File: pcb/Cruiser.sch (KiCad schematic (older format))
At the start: 42 parts, among them J1 USB-A, P1 BDM, SW1 Load, SW2 Reset, T2 T2, T3 T3, U1 FT232RL, U2 MC9S12XDP512, X1 16MHz

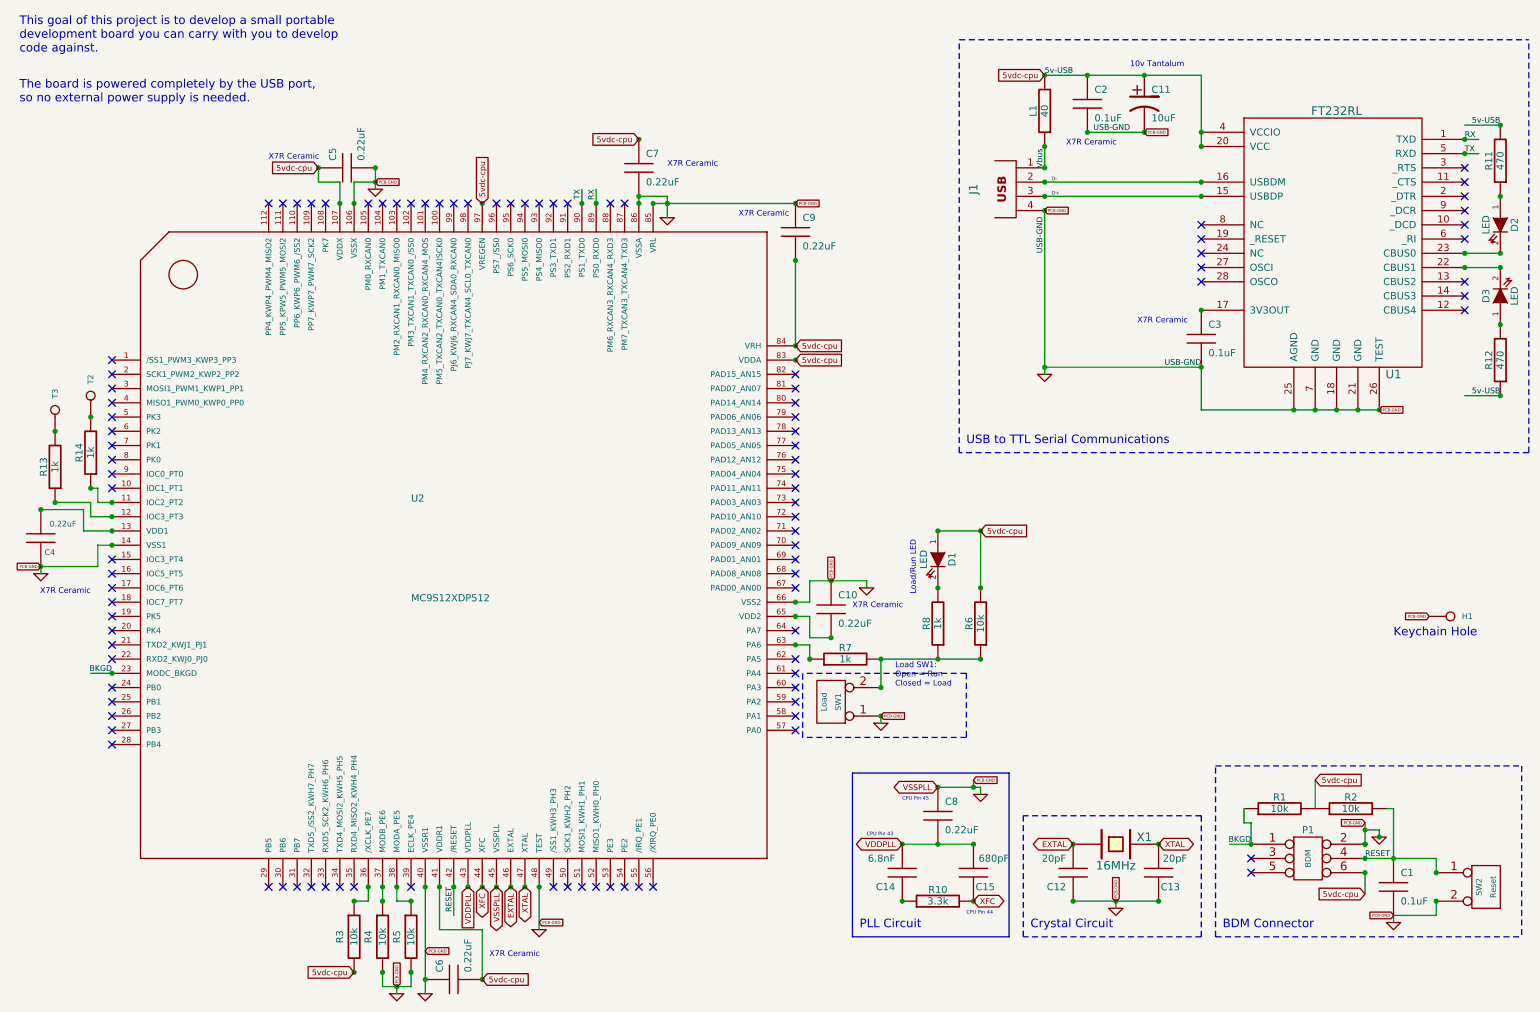
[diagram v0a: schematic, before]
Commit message: Added T0 and T1 outputs and their 1k resistors.
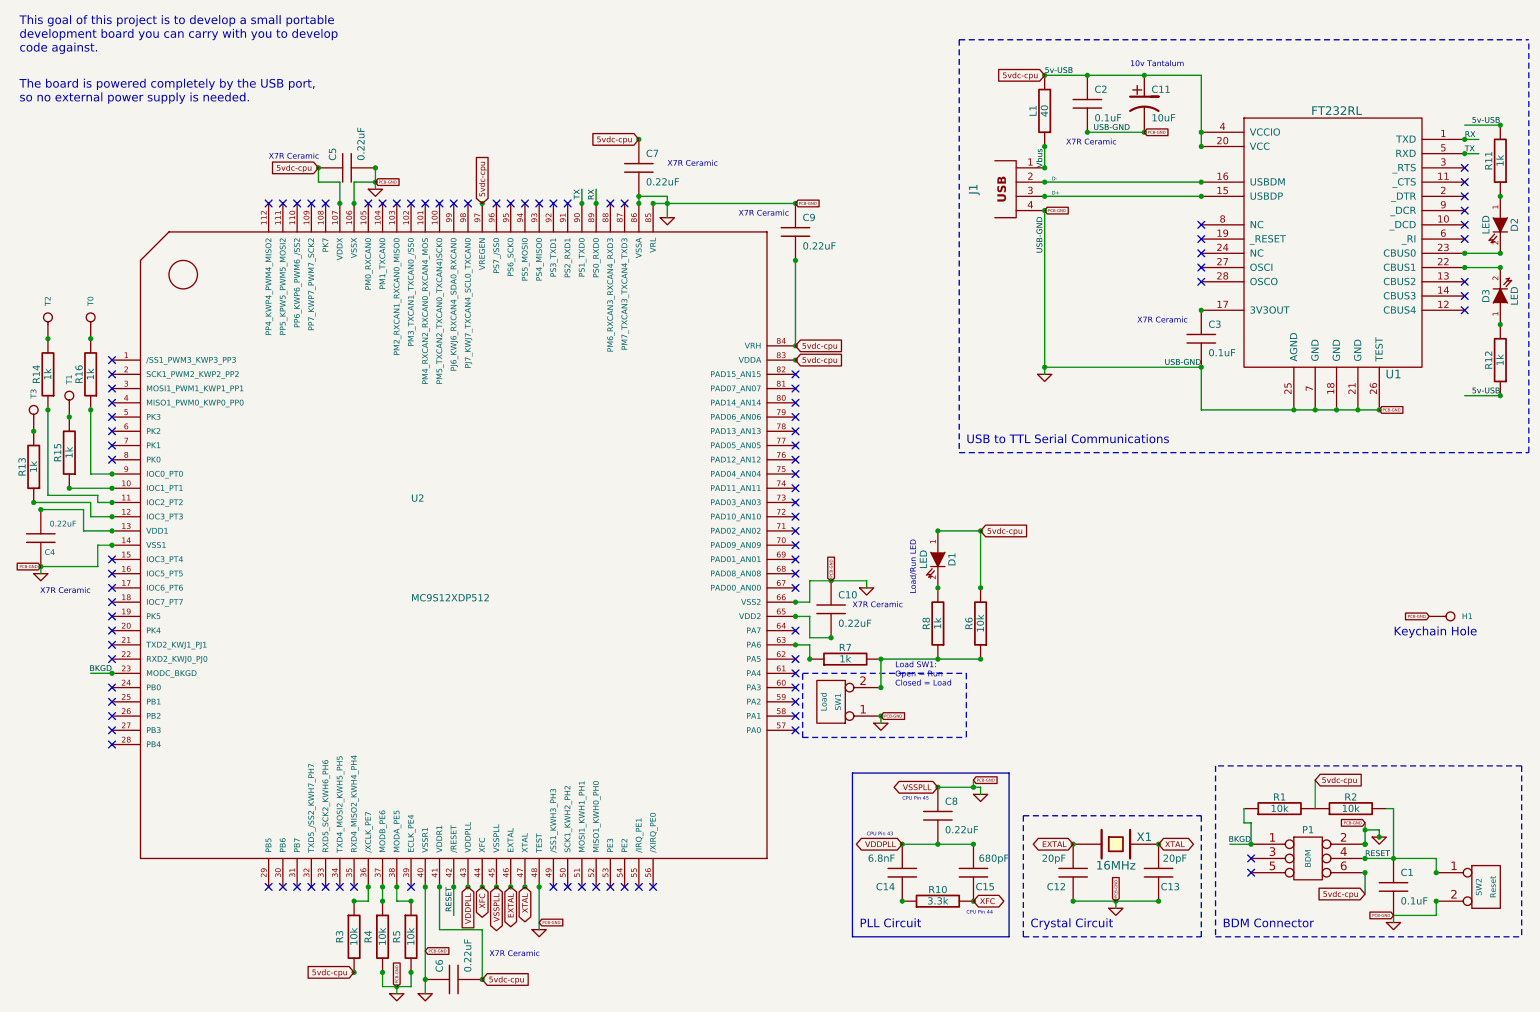
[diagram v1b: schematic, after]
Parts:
- added R15, R16: 1k, symbol R
- added T0: T0, symbol CONN_1
- added T1: T1, symbol CONN_1
- R11, R12: value 470 -> 1k
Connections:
- wire segments 94 -> 98
- no-connect marks 99 -> 97
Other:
- moved on the sheet: R13, R14, T2, T3
